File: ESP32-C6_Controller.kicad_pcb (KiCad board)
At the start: 2 copper layers, 15 x 25 mm, 0 parts

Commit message: - Change Copper Layer from 2 to 4
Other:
- copper layers 2 -> 4
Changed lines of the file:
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@@
 	(layers
 		(0 "F.Cu" signal)
+		(1 "In1.Cu" signal)
+		(2 "In2.Cu" signal)
 		(31 "B.Cu" signal)
 		(32 "B.Adhes" user "B.Adhesive")
@@
 	)
 	(setup
+		(stackup
+			(layer "F.SilkS"
+				(type "Top Silk Screen")
+			)
+			(layer "F.Paste"
+				(type "Top Solder Paste")
+			)
+			(layer "F.Mask"
+				(type "Top Solder Mask")
+				(thickness 0.01)
+			)
+			(layer "F.Cu"
+				(type "copper")
+				(thickness 0.035)
+			)
+			(layer "dielectric 1"
+				(type "prepreg")
+				(thickness 0.1)
+				(material "FR4")
+				(epsilon_r 4.5)
+				(loss_tangent 0.02)
+			)
+			(layer "In1.Cu"
+				(type "copper")
+				(thickness 0.035)
+			)
+			(layer "dielectric 2"
+				(type "core")
+				(thickness 1.24)
+				(material "FR4")
+				(epsilon_r 4.5)
+				(loss_tangent 0.02)
+			)
+			(layer "In2.Cu"
+				(type "copper")
+				(thickness 0.035)
+			)
+			(layer "dielectric 3"
+				(type "prepreg")
+				(thickness 0.1)
+				(material "FR4")
+				(epsilon_r 4.5)
+				(loss_tangent 0.02)
+			)
+			(layer "B.Cu"
+				(type "copper")
+				(thickness 0.035)
+			)
+			(layer "B.Mask"
+				(type "Bottom Solder Mask")
+				(thickness 0.01)
+			)
+			(layer "B.Paste"
+				(type "Bottom Solder Paste")
+			)
+			(layer "B.SilkS"
+				(type "Bottom Silk Screen")
+			)
+			(copper_finish "None")
+			(dielectric_constraints no)
+		)
 		(pad_to_mask_clearance 0)
 		(allow_soldermask_bridges_in_footprints no)

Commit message: import components
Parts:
- added C1: 0.1uF, Capacitor_SMD:C_0402_1005Metric, F.Cu at (108.0, 112.0)
- added C10: TBC, Capacitor_SMD:C_0603_1608Metric, F.Cu at (98.0, 99.7)
- added C11: TBC, Capacitor_SMD:C_0603_1608Metric, F.Cu at (98.0, 102.2)
- added C12: TBC, Capacitor_SMD:C_0603_1608Metric, F.Cu at (98.0, 104.7)
- added C13: 1uF, Capacitor_SMD:C_0402_1005Metric, F.Cu at (113.7, 115.9)
- added C14: 100n, Capacitor_SMD:C_0402_1005Metric, F.Cu at (137.0, 113.0)
- added C15: 100n, Capacitor_SMD:C_0402_1005Metric, F.Cu at (137.0, 115.0)
- added C16: 150p, Capacitor_SMD:C_0603_1608Metric, F.Cu at (137.2, 97.2)
- added C17: 22u, Capacitor_SMD:C_0805_2012Metric, F.Cu at (132.2, 107.5)
- added C18: 22u, Capacitor_SMD:C_0805_2012Metric, F.Cu at (132.2, 110.5)
- added C19: 1.5p, Capacitor_SMD:C_0603_1608Metric, F.Cu at (98.0, 107.2)
- added C2: 0.1uF, Capacitor_SMD:C_0402_1005Metric, F.Cu at (108.0, 114.0)
- added C21: 1.5p, Capacitor_SMD:C_0603_1608Metric, F.Cu at (98.0, 109.8)
- added C3: 0.1u, Capacitor_SMD:C_0402_1005Metric, F.Cu at (108.0, 115.9)
- added C4: 0.1uF, Capacitor_SMD:C_0402_1005Metric, F.Cu at (110.8, 112.0)
- added C5: 10nF, Capacitor_SMD:C_0402_1005Metric, F.Cu at (110.8, 114.0)
- added C6: 1uF, Capacitor_SMD:C_0402_1005Metric, F.Cu at (110.8, 115.9)
- added C7: 10nF, Capacitor_SMD:C_0402_1005Metric, F.Cu at (113.7, 112.0)
- added C8: 1uF, Capacitor_SMD:C_0402_1005Metric, F.Cu at (113.7, 114.0)
- added C9: TBC, Capacitor_SMD:C_0603_1608Metric, F.Cu at (98.0, 97.2)
- added E1: AMCA31-2R450G-S1F-T3, 1_ESP32:XDCR_AMCA31-2R450G-S1F-T3, F.Cu at (106.6, 122.9)
- added F1: Fuse_Small, Fuse:Fuse_1206_3216Metric, F.Cu at (132.8, 113.7)
- added FB1: BLM18KG121TN1D, Inductor_SMD:L_CommonModeChoke_Coilcraft_0603USB, F.Cu at (118.3, 115.4)
- added J1: USB4105-GF-A, 1_ESP32:GCT_USB4105-GF-A, F.Cu at (126.3, 102.7)
- added J2: Conn_01x12, Connector_PinSocket_2.54mm:PinSocket_1x12_P2.54mm_Vertical, F.Cu at (89.2, 98.3)
- added J3: Conn_01x12, Connector_PinSocket_2.54mm:PinSocket_1x12_P2.54mm_Vertical, F.Cu at (93.8, 98.3)
- added L1: 2nH, Inductor_SMD:L_0805_2012Metric, F.Cu at (111.7, 122.7)
- added L2: 2.4nH, Inductor_SMD:L_0805_2012Metric, F.Cu at (111.7, 125.4)
- added R1: TBC, Resistor_SMD:R_0402_1005Metric, F.Cu at (101.5, 97.0)
- added R10: 5.1k, Resistor_SMD:R_0603_1608Metric, F.Cu at (137.2, 104.7)
- added R11: 600, Resistor_SMD:R_0402_1005Metric, F.Cu at (135.9, 107.0)
- added R12: 1000, Resistor_SMD:R_0402_1005Metric, F.Cu at (135.9, 109.0)
- added R13: 0, Resistor_SMD:R_0402_1005Metric, F.Cu at (135.9, 111.0)
- added R2: 10k, Resistor_SMD:R_0402_1005Metric, F.Cu at (101.5, 98.9)
- added R3: 7.5M, Resistor_SMD:R_0402_1005Metric, F.Cu at (101.5, 100.9)
- added R4: 10k, Resistor_SMD:R_0402_1005Metric, F.Cu at (101.5, 102.9)
- added R5: 10k, Resistor_SMD:R_0402_1005Metric, F.Cu at (101.5, 104.9)
- added R6: 499, Resistor_SMD:R_0402_1005Metric, F.Cu at (101.5, 106.9)
- added R7: 499, Resistor_SMD:R_0402_1005Metric, F.Cu at (101.5, 108.9)
- added R8: 330, Resistor_SMD:R_0603_1608Metric, F.Cu at (137.2, 99.7)
- added R9: 5.1k, Resistor_SMD:R_0603_1608Metric, F.Cu at (137.2, 102.2)
- added SW1: SW_Push, 1_ESP32:SW4_PTS815 SJM 250 SMTR LFS_CNK, F.Cu at (108.2, 100.1)
- added SW2: SW_Push, 1_ESP32:SW4_PTS815 SJM 250 SMTR LFS_CNK, F.Cu at (108.2, 106.7)
- added TP1: TestPoint, TestPoint:TestPoint_Pad_1.5x1.5mm, F.Cu at (118.9, 97.7)
- added TP2: TestPoint, TestPoint:TestPoint_Pad_1.5x1.5mm, F.Cu at (118.9, 101.3)
- added TP3: TestPoint, TestPoint:TestPoint_Pad_1.5x1.5mm, F.Cu at (118.9, 104.8)
- added TP4: TestPoint, TestPoint:TestPoint_Pad_1.5x1.5mm, F.Cu at (118.9, 108.4)
- added TP5: TestPoint, TestPoint:TestPoint_Pad_1.5x1.5mm, F.Cu at (118.9, 111.9)
- added U1: ESP32-C6, Package_DFN_QFN:QFN-40-1EP_5x5mm_P0.4mm_EP3.6x3.6mm, F.Cu at (99.7, 121.7)
- added U2: W25Q16JVSSIQ, 1_ESP32:W25Q16JVSSIQ_WIN, F.Cu at (101.3, 114.5)
- added U3: AZ1117IH-3.3TRG1, 1_ESP32:SOT223_AZ1117I_6P5X3P5_DIO, F.Cu at (125.9, 110.9)
- added U4: ESD122DMYR, 1_ESP32:DMY0003A, F.Cu at (138.2, 107.2)
- added XTAL1: ECS-400-10-37B2-CKY-TR, 1_ESP32:ECX-1637B2_ECS, F.Cu at (106.2, 126.3)
- added XTAL2: SC32S-7PF20PPM, 1_ESP32:XTAL_SC32S-7PF20PPM_EPS, F.Cu at (106.8, 119.7)

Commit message: Layout update positions
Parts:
- C19, C21, E1, L2: moved to B.Cu
- moved U4 65.1 mm to (74.6, 93.4), turned to 180 degrees
- moved R10 65.1 mm to (73.0, 94.2), turned to 90 degrees
- moved J3 62.7 mm to (156.5, 98.3)
- moved R9 59.3 mm to (78.5, 94.2), turned to 90 degrees
- moved C16 57.0 mm to (80.2, 94.3), turned to -90 degrees
- moved R8 55.5 mm to (82.0, 94.2), turned to -90 degrees
- moved J2 52.8 mm to (142.0, 98.3)
- moved J1 51.5 mm to (77.5, 86.2), turned to 180 degrees
- moved L2 50.8 mm to (61.7, 116.8), turned to 180 degrees
- moved E1 45.5 mm to (61.0, 121.2), turned to 180 degrees
- moved C7 42.6 mm to (73.3, 98.5), turned to 90 degrees
- moved L1 42.4 mm to (74.0, 103.2), turned to 180 degrees
- moved C8 42.1 mm to (74.5, 98.5), turned to 90 degrees
- moved C6 39.1 mm to (75.8, 98.5), turned to 90 degrees
- moved C19 37.9 mm to (62.0, 118.8), turned to 180 degrees
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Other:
- board size 15 x 25 mm -> 18.5 x 32.5 mm

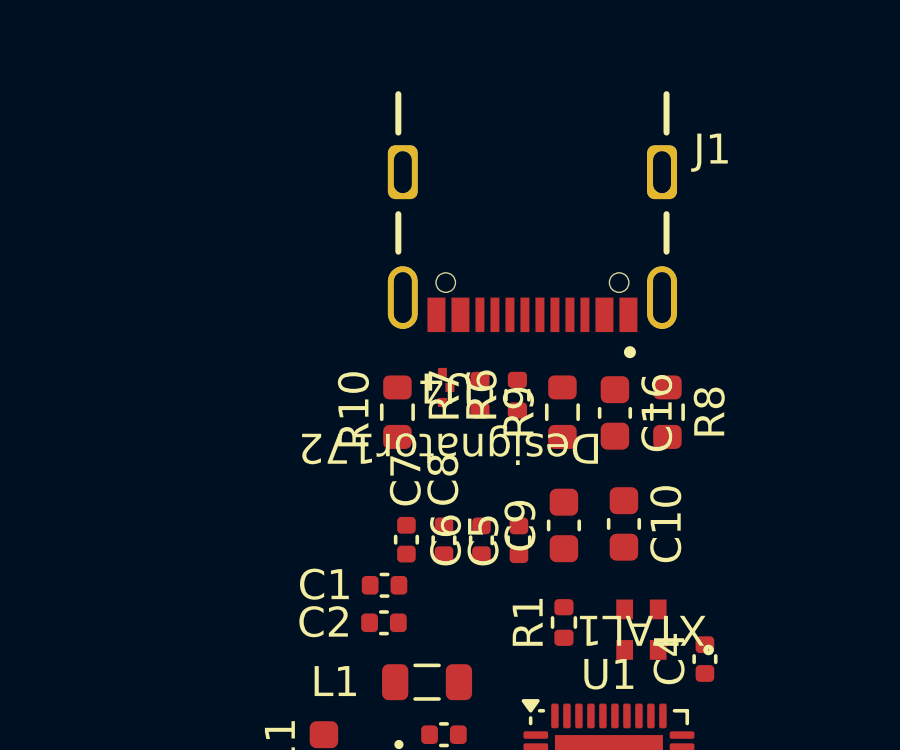
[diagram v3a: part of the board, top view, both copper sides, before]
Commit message: 4 layer to 6 layer
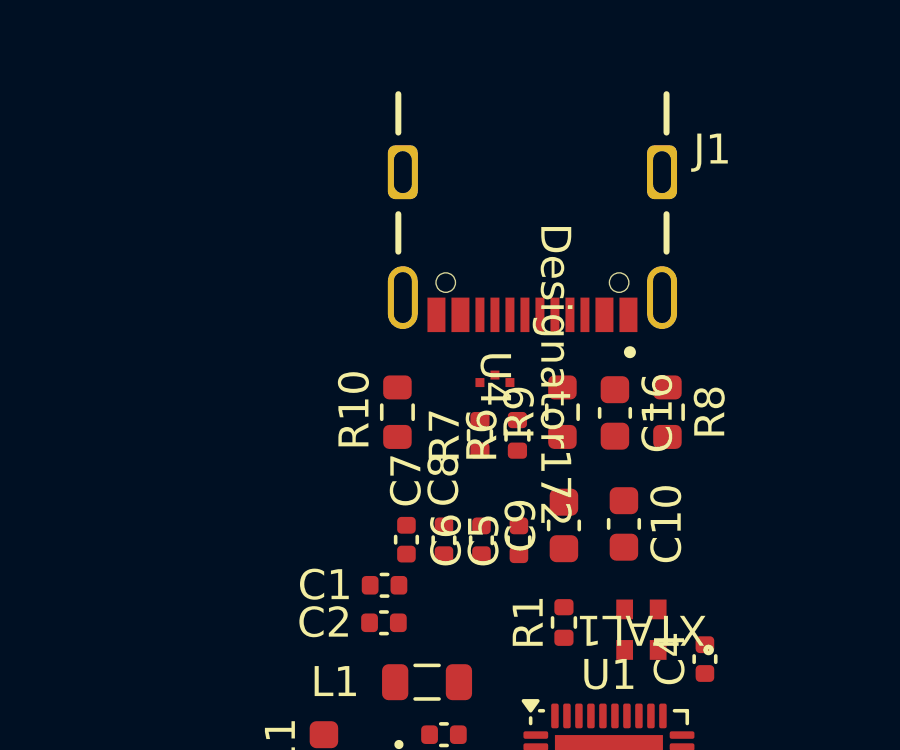
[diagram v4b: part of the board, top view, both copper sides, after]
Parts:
- moved U4 1.65 mm to (76.3, 93.1), turned to -90 degrees
- moved R6 1.34 mm to (77.0, 95.0)
- moved R7 1.34 mm to (75.8, 95.0)
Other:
- copper layers 4 -> 6

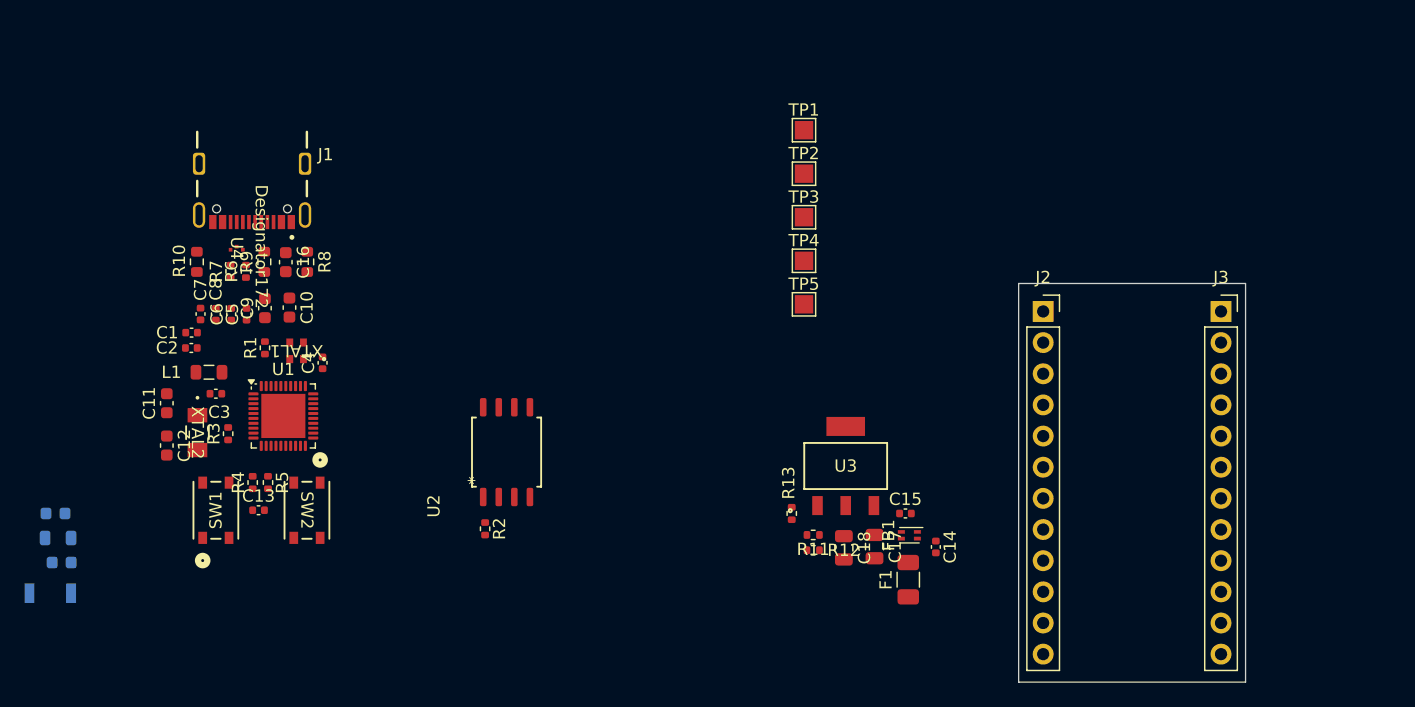
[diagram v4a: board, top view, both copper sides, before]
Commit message: Put components inside the board
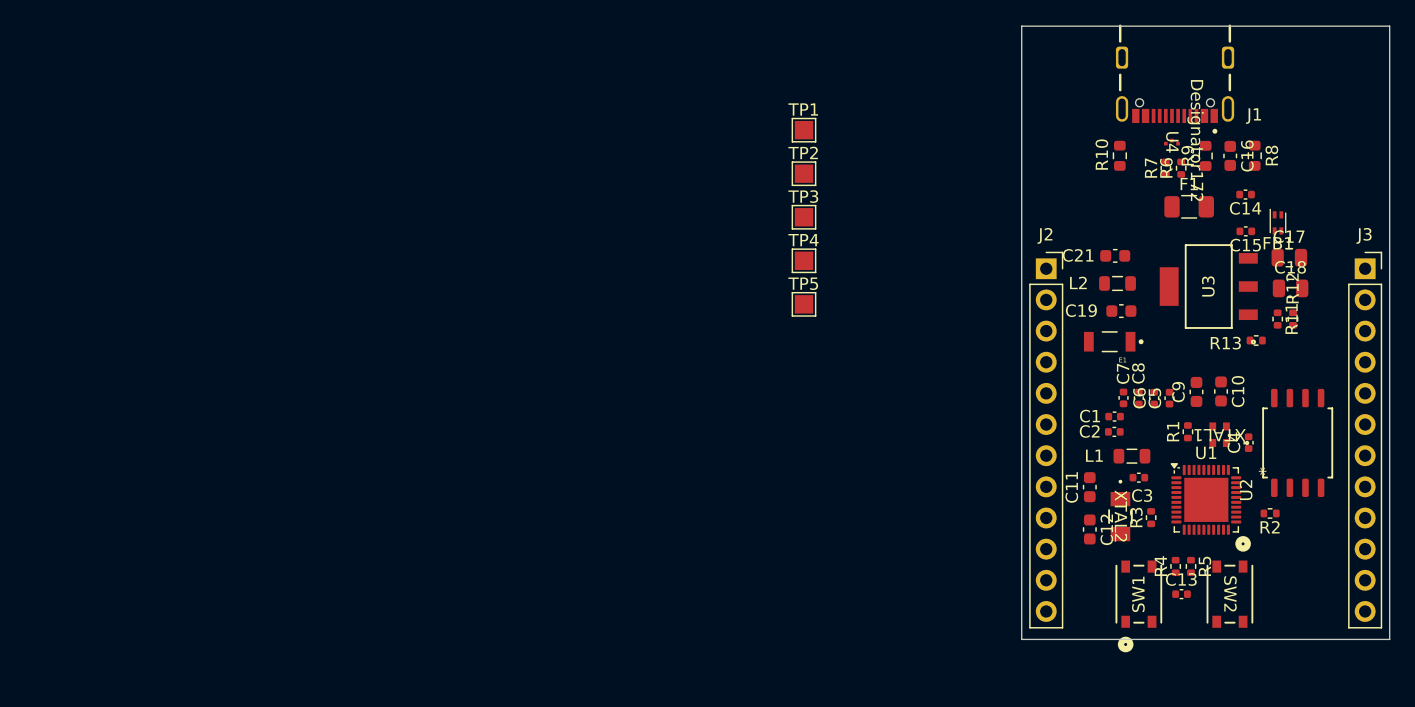
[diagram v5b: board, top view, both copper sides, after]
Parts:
- C19, C21, E1, L2: moved to F.Cu
- moved C21 88.9 mm to (147.9, 93.8)
- moved L2 88.8 mm to (148.1, 96.0)
- moved C19 88.8 mm to (148.4, 98.2)
- moved E1 88.8 mm to (147.4, 100.8)
- moved R8 77.7 mm to (159.2, 85.6)
- moved C16 77.5 mm to (157.2, 85.6)
- moved R9 77.2 mm to (155.2, 85.6)
- moved U4 76.7 mm to (152.5, 84.5)
- moved R6 76.7 mm to (153.2, 86.6)
- moved R7 76.7 mm to (152.0, 86.6)
- moved C10 76.3 mm to (156.5, 104.8)
- moved C9 76.3 mm to (154.5, 104.8)
- moved C4 75.8 mm to (158.8, 109.0)
- moved J1 75.7 mm to (152.8, 77.6)
- moved R10 75.7 mm to (148.2, 85.6)
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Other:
- board size 18.5 x 32.5 mm -> 30 x 50 mm

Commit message: Final position before routing
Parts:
- moved F1 7.37 mm to (147.0, 87.2), turned to -90 degrees
- moved C4 6.02 mm to (160.5, 114.8), turned to 0 degrees
- moved C2 2.44 mm to (146.0, 109.8)
- moved C5 2.26 mm to (153.5, 107.3)
- moved C6 2.12 mm to (152.0, 107.2)
- moved C8 2.02 mm to (150.5, 107.2)
- moved C7 1.97 mm to (149.0, 107.2)
- moved R10 1.80 mm to (149.8, 86.6)
- moved R8 1.50 mm to (160.8, 85.5)
- moved R2 1.50 mm to (160.5, 116.2)
- moved C9 1.32 mm to (154.5, 103.5)
- moved C10 1.28 mm to (156.5, 103.5)
- moved R1 1.25 mm to (155.0, 107.8)
- moved XTAL1 1.13 mm to (157.4, 107.9)
- moved C16 0.75 mm to (158.0, 85.6)
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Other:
- board text added: "${REFERENCE}"

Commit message: layout 80% done
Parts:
- moved J2 26.3 mm to (168.5, 95.2)
- moved J3 26.0 mm to (142.2, 95.0)
- moved R2 12.4 mm to (164.5, 104.5), turned to 0 degrees
- moved C4 9.56 mm to (159.2, 105.3), turned to 90 degrees
- moved C13 5.59 mm to (150.5, 116.5), turned to 90 degrees
- moved SW2 4.29 mm to (162.0, 120.3), turned to 180 degrees
- moved SW1 3.45 mm to (152.7, 120.2), turned to 180 degrees
- moved R3 3.42 mm to (150.8, 111.7)
- moved C10 3.24 mm to (159.5, 102.2), turned to 180 degrees
- moved C12 2.94 mm to (148.2, 117.7), turned to 90 degrees
- moved XTAL1 2.83 mm to (156.3, 105.3), turned to 0 degrees
- moved R5 2.75 mm to (153.5, 116.5), turned to 90 degrees
- moved R4 2.68 mm to (152.0, 116.5), turned to -90 degrees
- moved C1 2.55 mm to (146.7, 104.9)
- moved C5 2.55 mm to (152.5, 104.9)
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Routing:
- net 5V_Filtered: track 0.00 -> 28.1 mm
- net VDDSPI: track 0.00 -> 24.2 mm
- net GPIO11: track 0.00 -> 23.3 mm, vias 0 -> 1
- net SPICS: track 0.00 -> 19.7 mm, vias 0 -> 2
- net GPIO10: track 0.00 -> 19.5 mm, vias 0 -> 1
- net SPIQ: track 0.00 -> 17.3 mm, vias 0 -> 2
- net /USB_C Power Circuit/5V_USB: track 0.00 -> 17.1 mm
- net 3V3: track 0.00 -> 15.9 mm
- net SPIWP: track 0.00 -> 14.7 mm, vias 0 -> 2
- net GPIO09: track 0.00 -> 13.3 mm
- net Net-(J1-VBUS): track 0.00 -> 13.1 mm
- net RTC_Xin: track 0.00 -> 10.8 mm
- net Net-(C2-Pad1): track 0.00 -> 10.5 mm, vias 0 -> 2
- net SPIHOLD: track 0.00 -> 10.4 mm
- net Xout: track 0.00 -> 10.0 mm
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- added copper zone on F.Cu, net 3V3
- added copper zone on F.Cu, net GND1
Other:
- board text added: "Check DP1 and DN1 length? why DP2 and DN2"

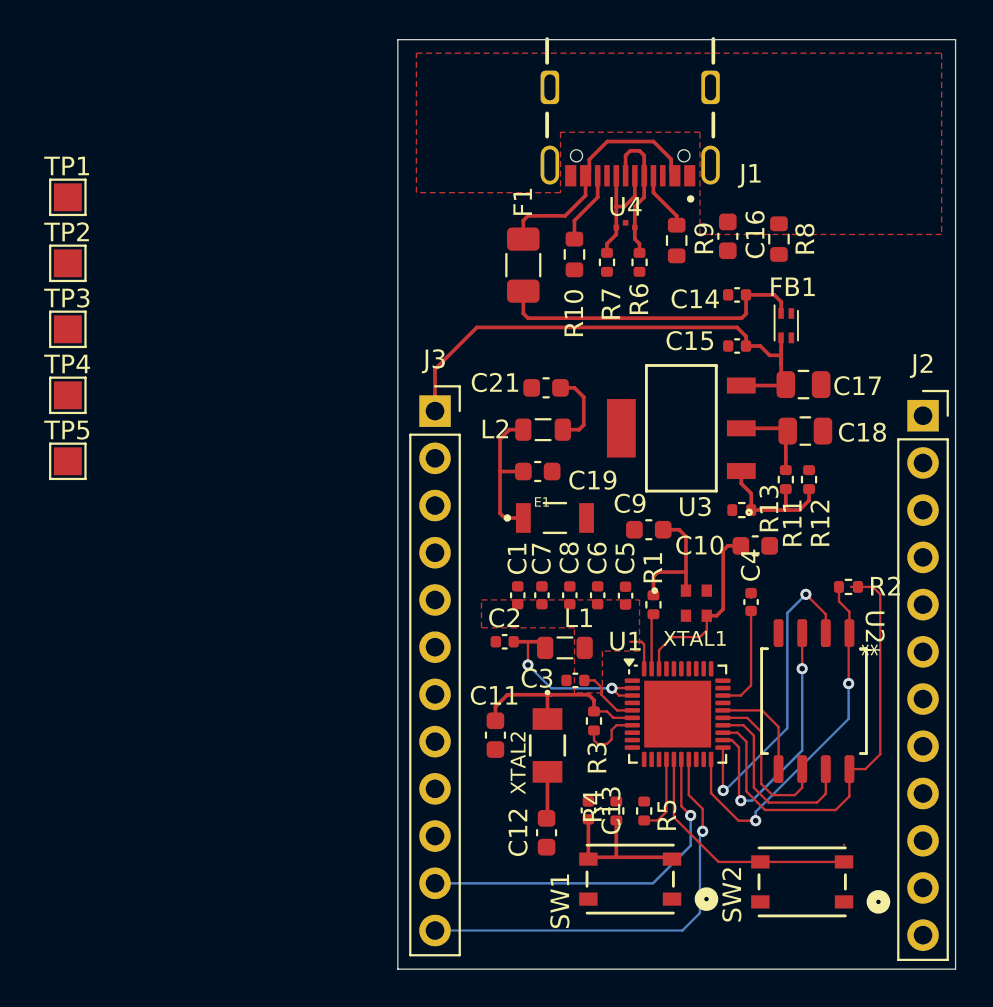
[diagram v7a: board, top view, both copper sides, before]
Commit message: Trace completed, leave comments for tasks
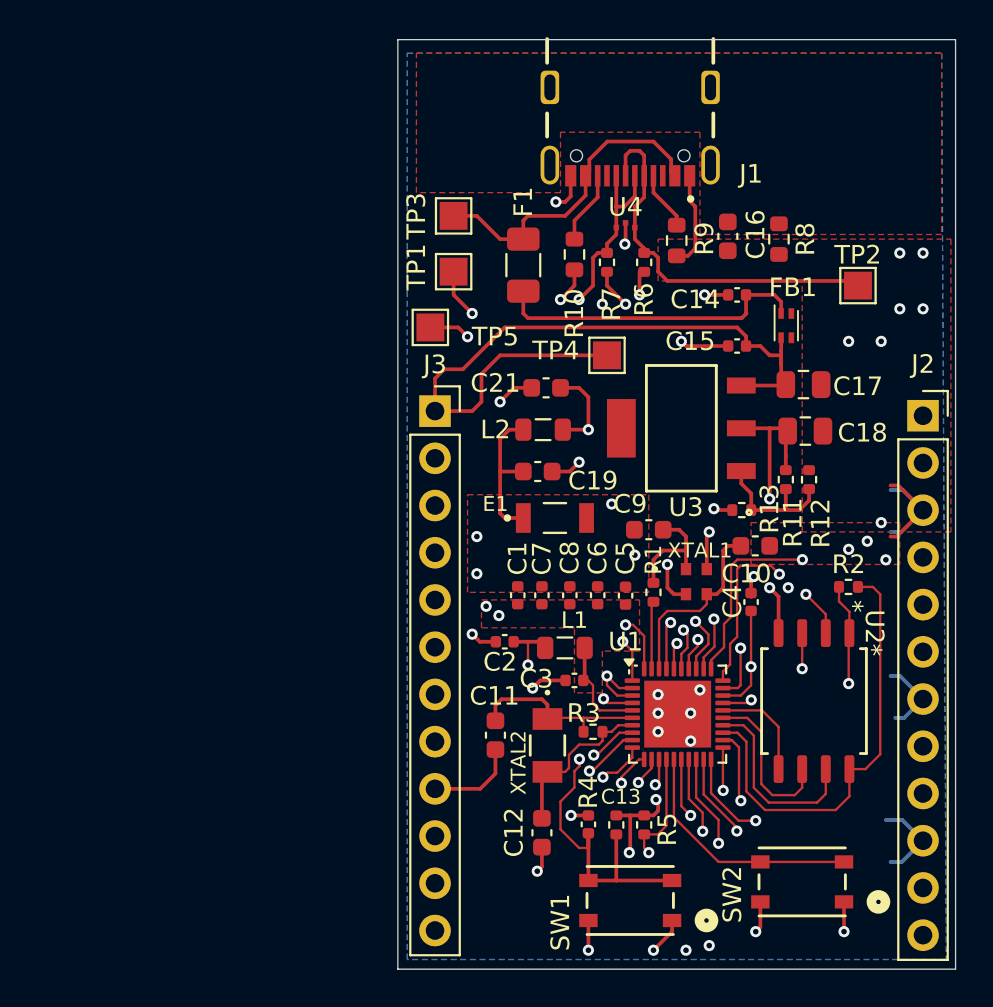
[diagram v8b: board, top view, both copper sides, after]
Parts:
- moved TP2 42.5 mm to (165.0, 88.2)
- moved TP4 29.1 mm to (151.5, 92.0)
- moved TP3 21.6 mm to (143.2, 84.5)
- moved TP1 21.1 mm to (143.2, 87.5)
- moved TP5 20.8 mm to (142.0, 90.5)
- moved XTAL1 1.16 mm to (156.3, 104.2)
- moved SW1 1.15 mm to (152.7, 121.3)
- moved C13 0.75 mm to (150.5, 117.2)
- moved R4 0.75 mm to (152.0, 117.3)
- moved R5 0.75 mm to (153.5, 117.3)
- moved R1 0.67 mm to (154.0, 104.8)
- moved R3 0.58 mm to (150.8, 112.2), turned to 180 degrees
- moved C12 0.25 mm to (148.0, 117.7)
- moved R6 0.25 mm to (153.5, 87.0)
- moved C3 0.05 mm to (149.8, 109.5)
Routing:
- net GND: track 0.06 -> 74.8 mm, vias 0 -> 39
- net Net-(U1-GPIO12/USB_D-): track 0.00 -> 41.3 mm, vias 0 -> 3
- net Net-(U1-GPIO13/USB_D+): track 0.00 -> 38.5 mm, vias 0 -> 2
- net GPIO22: track 0.00 -> 34.7 mm, vias 0 -> 2
- net GPIO23: track 0.00 -> 30.1 mm, vias 0 -> 2
- net 3V3: track 15.9 -> 44.4 mm, vias 0 -> 9
- net GPIO02: track 0.00 -> 21.5 mm, vias 0 -> 1
- net GPIO03: track 0.00 -> 20.6 mm, vias 0 -> 1
- net TX: track 0.00 -> 20.3 mm, vias 0 -> 1
- net RX: track 0.00 -> 19.1 mm, vias 0 -> 1
- net GPIO20: track 0.00 -> 18.1 mm, vias 0 -> 1
- net MTMS: track 0.00 -> 17.9 mm, vias 0 -> 1
- net GPIO18: track 0.00 -> 17.7 mm, vias 0 -> 2
- net GPIO21: track 0.00 -> 17.4 mm, vias 0 -> 1
- net MTDI: track 0.00 -> 16.5 mm, vias 0 -> 1
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- added copper zone on In4.Cu, net 3V3
- added copper zone on B.Cu, net GND
- added copper zone on F.Cu, net GND
- added copper zone on In1.Cu, net GND
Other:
- board text added: "-Check DP1 and DN1 length? -why DP2 and DN2 -Increase trace width for power"
- board text removed: "Check DP1 and DN1 length? why DP2 and DN2"
